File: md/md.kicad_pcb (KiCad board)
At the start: 2 copper layers, 49.5 x 70.5 mm, 53 parts, among them J1 ControlPort, J2 Conn_01x01, J3 Conn_02x08_Counter_Clockwise, J4 Conn_02x08_Counter_Clockwise, J5 Conn_01x01, J6 Conn_02x08_Counter_Clockwise, J7 Conn_02x08_Counter_Clockwise, J8 12v, Q1 FET_A_UP, Q2 FET_A_DOWN, Q3 FET_B_UP, Q4 FET_B_DOWN, U1 7400, U2 IRS2302, U3 TLP2955, U4 TLP2955, U5 IRS2302, U6 LM7812

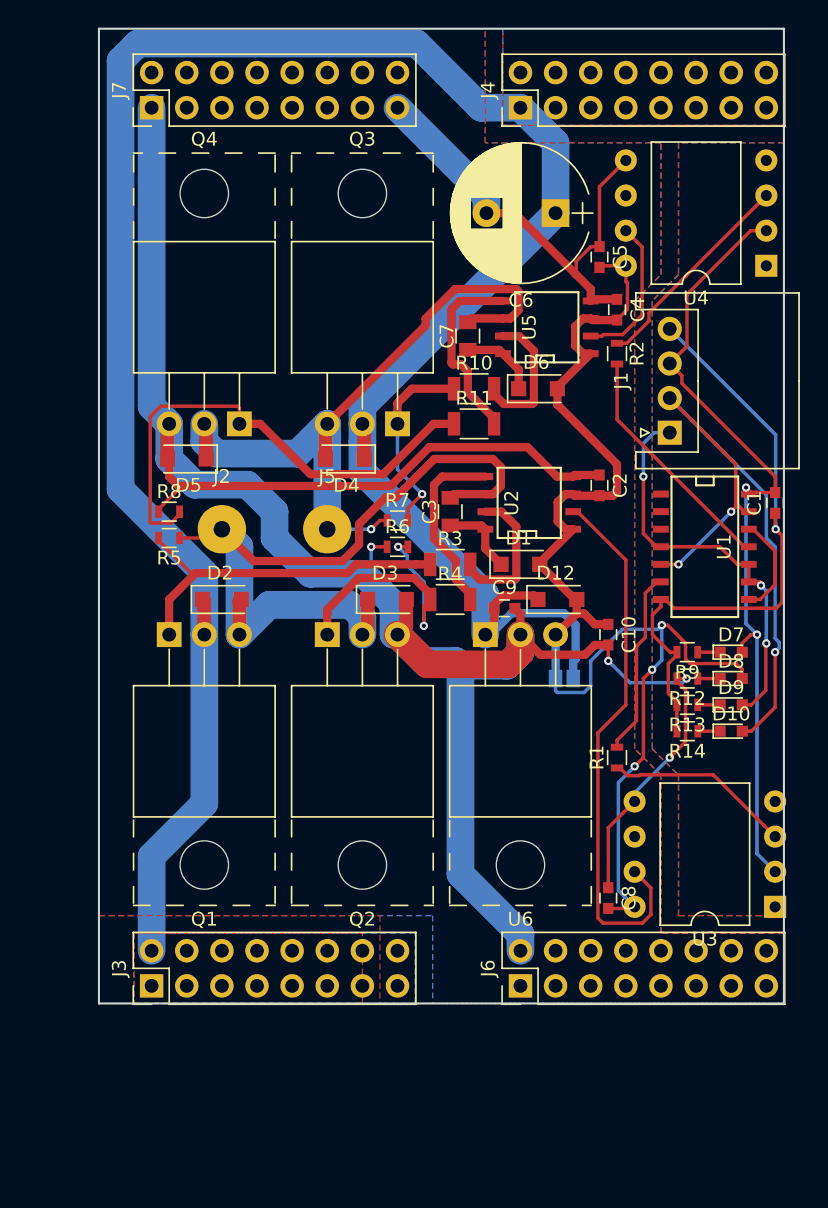
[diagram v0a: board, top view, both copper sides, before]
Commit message: use TLP2105
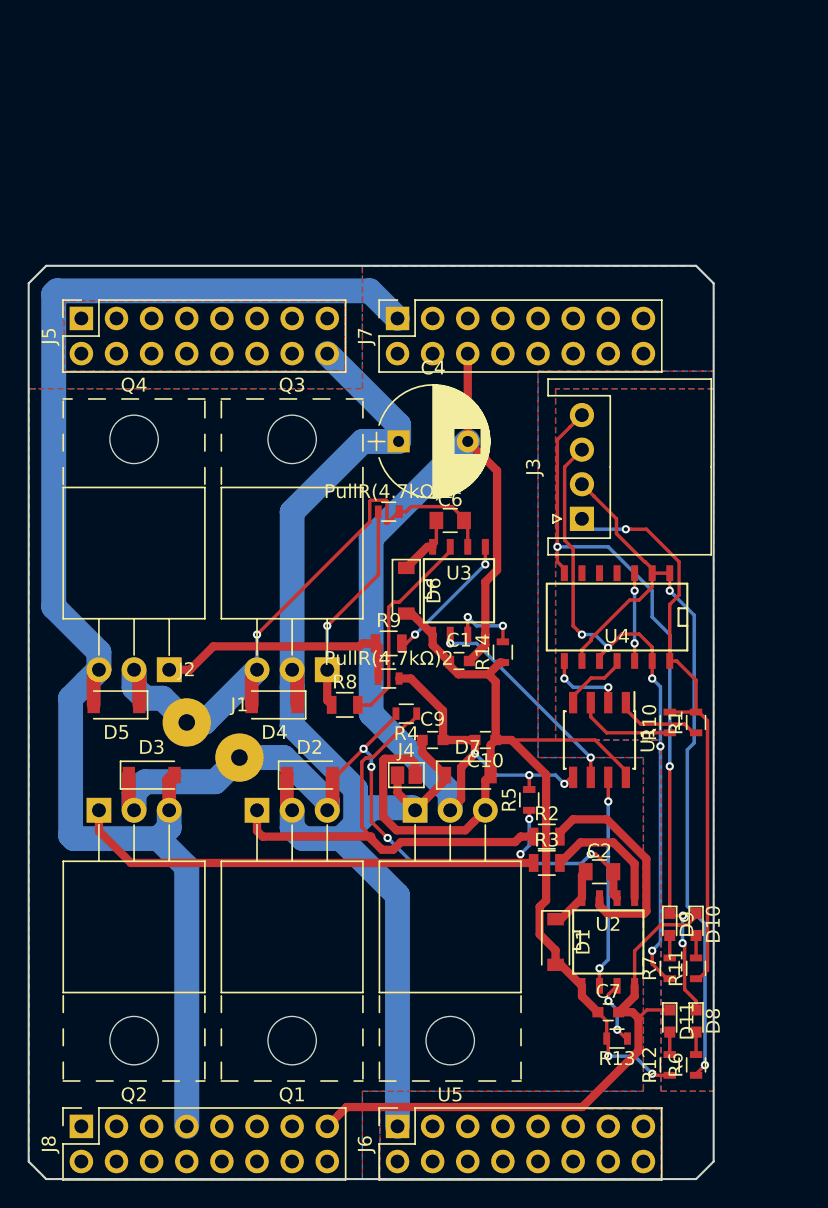
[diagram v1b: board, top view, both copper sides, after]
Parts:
- removed C3: bootC, Capacitors_SMD:C_0805
- removed C5, C8: passC, Capacitors_SMD:C_0603
- removed D12: RegRevD, Diodes_SMD:D_SOD-123F
- removed U6: LM7812, TO_SOT_Packages_THT:TO-220-3_Horizontal_Reversed
- added D11: SML-E12V8WT86, LEDs:LED_0603, F.Cu at (173.4, 149.9)
- added PullR(4.7kΩ)1: R, Resistors_SMD:R_0603, F.Cu at (153.0, 113.0)
- added PullR(4.7kΩ)2: R, Resistors_SMD:R_0603, F.Cu at (153.0, 125.1)
- C1: value passC -> 0.1uF
- C10: value RegOutC -> 1uF
- C2: value passC -> 10uF; footprint Capacitors_SMD:C_0603 -> Capacitors_SMD:C_0805
- C4: value passC -> CP; footprint Capacitors_SMD:C_0603 -> Capacitors_THT:CP_Radial_D8.0mm_P5.00mm
- C6: value PowerCP -> 10uF; footprint Capacitors_THT:CP_Radial_D10.0mm_P5.00mm -> Capacitors_SMD:C_0805
- C7: value bootC -> 0.1uF; footprint Capacitors_SMD:C_0805 -> Capacitors_SMD:C_0603
- C9: value RegInC -> 1uF
- D1, D6: value bootD -> SS2040FL; footprint Diodes_SMD:D_SOD-123F -> Diodes_SMD:D_SOD-123
- D10: value LED -> SML-E12P8T86
- D2, D3, D4, D5: value RevD -> SS2040FL; footprint Diodes_SMD:D_SOD-123F -> Diodes_SMD:D_SOD-123
- D7: value LED -> SS2040FL; footprint LEDs:LED_0603 -> Diodes_SMD:D_SOD-123
- D8: value LED -> SML-E12Y8WT86
- D9: value LED -> SML-E13BC8TT86
- J1: value ControlPort -> OutB; footprint Connectors_JST:JST_XH_S04B-XH-A_04x2.50mm_Angled -> Wire_Pads:SolderWirePad_single_1-2mmDrill
- J2: value Conn_01x01 -> OutA
- J3: value Conn_02x08_Counter_Clockwise -> Conn_01x04; footprint Pin_Headers:Pin_Header_Straight_2x08_Pitch2.54mm -> Connectors_JST:JST_XH_S04B-XH-A_04x2.50mm_Angled
- J4: value Conn_02x08_Counter_Clockwise -> GS2; footprint Pin_Headers:Pin_Header_Straight_2x08_Pitch2.54mm -> Connectors:GS2
- J5: value Conn_01x01 -> Conn_02x08_Counter_Clockwise; footprint Wire_Pads:SolderWirePad_single_1-2mmDrill -> Socket_Strips:Socket_Strip_Straight_2x08_Pitch2.54mm
- J6, J7: footprint Pin_Headers:Pin_Header_Straight_2x08_Pitch2.54mm -> Socket_Strips:Socket_Strip_Straight_2x08_Pitch2.54mm
- J8: value 12v -> Conn_02x08_Counter_Clockwise; footprint Connectors:GS2 -> Socket_Strips:Socket_Strip_Straight_2x08_Pitch2.54mm; moved to F.Cu
- Q1: value FET_A_UP -> IRFB7437PBF
- Q2: value FET_A_DOWN -> IRFB7437PBF
- Q3: value FET_B_UP -> IRFB7437PBF
- Q4: value FET_B_DOWN -> IRFB7437PBF
- R1: value tlp-in-R -> TLP_R(470Ω)
- R10: value GateR -> TLP_R(470Ω); footprint Resistors_SMD:R_1206 -> Resistors_SMD:R_0603
- R11: value GateR -> LEDR(470Ω); footprint Resistors_SMD:R_1206 -> Resistors_SMD:R_0603
- R12: value R -> LEDR(1.2kΩ)
- R13: value R -> PullR
- R2: value tlp-in-R -> GateR(6.8Ω); footprint Resistors_SMD:R_0603 -> Resistors_SMD:R_0805
- R3: value GateR -> GateR(6.8Ω); footprint Resistors_SMD:R_1206 -> Resistors_SMD:R_0805
- R4: value GateR -> PullR(4.7kΩ); footprint Resistors_SMD:R_1206 -> Resistors_SMD:R_0603
- R5: value PullR -> PullR(4.7kΩ)
- R6, R7: value PullR -> LEDR(470Ω)
- R8: value PullR -> GateR(6.8Ω); footprint Resistors_SMD:R_0603 -> Resistors_SMD:R_0805
- R9: value LEDR -> GateR(6.8Ω); footprint Resistors_SMD:R_0603 -> Resistors_SMD:R_0805
- U1: value 7400 -> TLP2105; footprint SMD_Packages:SOIC-14_N -> Housings_SOIC:SOIC-8_3.9x4.9mm_Pitch1.27mm
- U3: value TLP2955 -> IRS2302; footprint Housings_DIP:DIP-8_W10.16mm -> SMD_Packages:SOIC-8-N
- U4: value TLP2955 -> 7400; footprint Housings_DIP:DIP-8_W10.16mm -> SMD_Packages:SOIC-14_N
- U5: value IRS2302 -> L7812; footprint SMD_Packages:SOIC-8-N -> TO_SOT_Packages_THT:TO-220-3_Horizontal_Reversed
- moved C7 49.9 mm to (168.9, 149.2), turned to 0 degrees
- moved J4 49.0 mm to (154.3, 132.1)
- moved J8 47.6 mm to (130.8, 157.5), turned to 90 degrees
- moved J3 45.9 mm to (167.0, 113.5)
- moved R6 43.2 mm to (175.3, 153.0), turned to 90 degrees
- moved R11 42.5 mm to (175.3, 146.1), turned to 90 degrees
- moved J1 39.0 mm to (142.2, 130.8), turned to 0 degrees
- moved R7 37.9 mm to (173.4, 146.1), turned to 90 degrees
- moved U5 36.2 mm to (154.9, 134.6), turned to 0 degrees
- moved R2 35.3 mm to (164.5, 136.5), turned to 0 degrees
- moved U3 32.3 mm to (158.1, 118.7), turned to 0 degrees
- moved U2 32.3 mm to (168.9, 144.1), turned to 0 degrees
- moved R5 32.2 mm to (163.2, 133.9), turned to 90 degrees
- moved R10 28.0 mm to (173.4, 128.3), turned to 90 degrees
- moved R12 28.0 mm to (173.4, 153.0), turned to 90 degrees
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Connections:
- C1 pad 1: GND -> +12V
- C1 pad 2: +5V -> GNDPWR
- C2 pad 1: GNDPWR -> Net-(C2-Pad1)
- C2 pad 2: +12V -> Net-(C2-Pad2)
- C4 pad 1: GNDPWR -> +24V
- C4 pad 2: +12V -> GNDPWR
- C6 pad 1: +24V -> Net-(C6-Pad1)
- C6 pad 2: GNDPWR -> Net-(C6-Pad2)
- C7 pad 1: Net-(C7-Pad1) -> +12V
- C7 pad 2: Net-(C7-Pad2) -> GNDPWR
- D1 pad 1: Net-(C3-Pad1) -> Net-(C2-Pad1)
- D10 pad 1: Net-(D10-Pad1) -> GNDPWR
- D10 pad 2: /PWM -> Net-(D10-Pad2)
- D2 pad 2: Net-(C3-Pad2) -> Net-(C2-Pad2)
- D3 pad 1: Net-(C3-Pad2) -> Net-(C2-Pad2)
- D4 pad 2: Net-(C7-Pad2) -> Net-(C6-Pad2)
- D5 pad 1: Net-(C7-Pad2) -> Net-(C6-Pad2)
- D6 pad 1: Net-(C7-Pad1) -> Net-(C6-Pad1)
- D7 pad 1: Net-(D7-Pad1) -> +24V
- D7 pad 2: +5V -> +12V
- D8 pad 1: Net-(D8-Pad1) -> GND
- D8 pad 2: +12V -> Net-(D8-Pad2)
- D9 pad 1: Net-(D9-Pad1) -> GND
- D9 pad 2: /DIR -> Net-(D9-Pad2)
- J1 pad 1: /DIR -> Net-(C2-Pad2)
- J2 pad 1: Net-(C3-Pad2) -> Net-(C6-Pad2)
- J3 pad 1: +24V -> +5V
- J3 pad 2: +24V -> /DIR
- J3 pad 3: +24V -> /PWM
- J3 pad 4: +24V -> GND
- J4 pad 2: +24V -> +12V
- J5 pad 1: Net-(C7-Pad2) -> +24V
- J6 pad 1: GNDPWR -> +24V
- J6 pad 10: GNDPWR -> +24V
- J6 pad 11: GNDPWR -> +24V
- J6 pad 12: GNDPWR -> +24V
- J6 pad 13: GNDPWR -> +24V
- J6 pad 14: GNDPWR -> +24V
- J6 pad 15: GNDPWR -> +24V
- J6 pad 16: GNDPWR -> +24V
- J6 pad 2: GNDPWR -> +24V
- J6 pad 3: GNDPWR -> +24V
- J6 pad 4: GNDPWR -> +24V
- J6 pad 5: GNDPWR -> +24V
- J6 pad 6: GNDPWR -> +24V
- J6 pad 7: GNDPWR -> +24V
- J6 pad 8: GNDPWR -> +24V
- J6 pad 9: GNDPWR -> +24V
- J8 pad 1: +12V -> GNDPWR
- J8 pad 2: +24V -> GNDPWR
- Q1 pad 3: Net-(C3-Pad2) -> Net-(C2-Pad2)
- Q2 pad 2: Net-(C3-Pad2) -> Net-(C2-Pad2)
- Q3 pad 1: Net-(Q3-Pad1) -> Net-(PullR(4.7kΩ)1-Pad1)
- Q3 pad 3: Net-(C7-Pad2) -> Net-(C6-Pad2)
- Q4 pad 1: Net-(Q4-Pad1) -> Net-(PullR(4.7kΩ)2-Pad1)
- Q4 pad 2: Net-(C7-Pad2) -> Net-(C6-Pad2)
- R1 pad 2: Net-(R1-Pad2) -> +5V
- R10 pad 1: Net-(Q3-Pad1) -> Net-(R10-Pad1)
- R10 pad 2: Net-(R10-Pad2) -> +5V
- R11 pad 1: Net-(Q4-Pad1) -> +5V
- R11 pad 2: Net-(R11-Pad2) -> Net-(D10-Pad2)
- R12 pad 1: Net-(D8-Pad1) -> +12V
- R12 pad 2: GNDPWR -> Net-(D11-Pad2)
- R13 pad 1: Net-(D9-Pad1) -> Net-(R13-Pad1)
- R13 pad 2: GND -> +12V
- R14 pad 1: Net-(D10-Pad1) -> +12V
- R14 pad 2: GND -> Net-(R14-Pad2)
- R2 pad 1: Net-(R2-Pad1) -> Net-(Q1-Pad1)
- R3 pad 1: Net-(Q1-Pad1) -> Net-(Q2-Pad1)
- R4 pad 1: Net-(Q2-Pad1) -> Net-(Q1-Pad1)
- R4 pad 2: Net-(R4-Pad2) -> Net-(C2-Pad2)
- R5 pad 1: Net-(C3-Pad2) -> Net-(Q2-Pad1)
- R5 pad 2: Net-(Q1-Pad1) -> GNDPWR
- R6 pad 1: GNDPWR -> /DIR
- R6 pad 2: Net-(Q2-Pad1) -> Net-(D8-Pad2)
- R7 pad 1: Net-(C7-Pad2) -> /PWM
- R7 pad 2: Net-(Q3-Pad1) -> Net-(D9-Pad2)
- R8 pad 1: GNDPWR -> Net-(PullR(4.7kΩ)1-Pad1)
- R8 pad 2: Net-(Q4-Pad1) -> Net-(R8-Pad2)
- R9 pad 1: Net-(D7-Pad1) -> Net-(PullR(4.7kΩ)2-Pad1)
- R9 pad 2: GND -> Net-(R9-Pad2)
- U1 pad 1: Net-(U1-Pad1) -> Net-(R1-Pad1)
- U1 pad 3: Net-(U1-Pad3) -> Net-(R10-Pad1)
- U1 pad 4: /DIR -> Net-(U1-Pad4)
- U1 pad 5: /PWM -> GNDPWR
- U1 pad 6: Net-(R1-Pad2) -> /OUTB
- U1 pad 7: GND -> /OUTA
- U1 pad 8: Net-(U1-Pad12) -> +12V
- U2 pad 2: OUTA -> /OUTA
- U2 pad 3: +12V -> Net-(R13-Pad1)
- U2 pad 5: Net-(R4-Pad2) -> Net-(R3-Pad2)
- U2 pad 6: Net-(C3-Pad2) -> Net-(C2-Pad2)
- U2 pad 7: Net-(R3-Pad2) -> Net-(R2-Pad2)
- U2 pad 8: Net-(C3-Pad1) -> Net-(C2-Pad1)
- U3 pad 1: (no net) -> +12V
- U3 pad 2: +5V -> /OUTB
- U3 pad 3: Net-(R1-Pad1) -> Net-(R14-Pad2)
- U3 pad 4: (no net) -> GNDPWR
- U3 pad 5: GNDPWR -> Net-(R9-Pad2)
- U3 pad 6: (no net) -> Net-(C6-Pad2)
- U3 pad 7: OUTA -> Net-(R8-Pad2)
- U3 pad 8: +12V -> Net-(C6-Pad1)
- U4 pad 1: (no net) -> /DIR
- U4 pad 2: +5V -> /DIR
- U4 pad 3: Net-(R2-Pad1) -> Net-(U4-Pad12)
- U4 pad 4: (no net) -> Net-(U4-Pad4)
- U4 pad 5: GNDPWR -> Net-(U4-Pad5)
- U4 pad 6: (no net) -> Net-(U4-Pad6)
- U4 pad 7: OUTB -> GND
- U4 pad 8: +12V -> Net-(U1-Pad2)
- U5 pad 1: +12V -> +24V
- U5 pad 2: OUTB -> GNDPWR
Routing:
- net +24V: track 171.1 -> 91.9 mm
- net Net-(C3-Pad2): track 59.4 -> 0.00 mm
- net Net-(C2-Pad2): track 0.00 -> 57.3 mm, vias 0 -> 4
- net Net-(C7-Pad2): track 52.4 -> 0.00 mm, vias 1 -> 0
- net Net-(C6-Pad2): track 0.00 -> 45.3 mm, vias 0 -> 1
- net OUTA: track 39.8 -> 0.00 mm
- net Net-(Q4-Pad1): track 36.7 -> 0.00 mm
- net /DIR: track 29.6 -> 56.7 mm, vias 3 -> 2
- net Net-(PullR(4.7kΩ)2-Pad1): track 0.00 -> 18.3 mm
- net Net-(Q2-Pad1): track 20.3 -> 38.0 mm
- net +5V: track 58.9 -> 42.6 mm, vias 2 -> 1
- net /OUTB: track 0.00 -> 15.6 mm, vias 0 -> 2
- net Net-(PullR(4.7kΩ)1-Pad1): track 0.00 -> 15.6 mm, vias 0 -> 1
- net Net-(R2-Pad1): track 15.6 -> 0.00 mm
- net /OUTA: track 0.00 -> 15.3 mm, vias 0 -> 2
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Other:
- board size 49.5 x 70.5 mm -> 49.5 x 66 mm

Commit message: だいたい配置出来た
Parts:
- added C11: C, Capacitors_SMD:C_0603, F.Cu at (212.7, 78.1)
- added C3: PowerC, Capacitors_THT:C_Disc_D5.0mm_W2.5mm_P5.00mm, F.Cu at (207.0, 88.9)
- added C5: PowerC, Capacitors_THT:C_Disc_D5.0mm_W2.5mm_P5.00mm, F.Cu at (209.6, 95.2)
- added C8: C, Capacitors_SMD:C_0603, F.Cu at (229.9, 88.3)
- C10: value 1uF -> RegOutC(1uF)
- C2, C6: value 10uF -> BootC(10uF); footprint Capacitors_SMD:C_0805 -> Capacitors_SMD:C_1206
- C4: value CP -> PowerCP
- C9: value 1uF -> RegInC(1uF)
- D10: value SML-E12P8T86 -> 5VLED(SML-E12P8T86)
- D11: value SML-E12V8WT86 -> 12VLED(SML-E12V8WT86)
- D2, D3, D4, D5: value SS2040FL -> RevD(SS2040FL)
- D7: value SS2040FL -> RegRevC(SS2040FL)
- D8: value SML-E12Y8WT86 -> DIRLED(SML-E12Y8WT86)
- D9: value SML-E13BC8TT86 -> LED(SML-E13BC8TT86)
- J3: value Conn_01x04 -> Interface
- J4: value GS2 -> 12VJmp
- Q1, Q2: value IRFB7437PBF -> FETA(IRFB7437PBF)
- Q3, Q4: value IRFB7437PBF -> FETB(IRFB7437PBF)
- R11: value LEDR(470Ω) -> 5VLEDR(470Ω)
- R12: value LEDR(1.2kΩ) -> 12VLEDR(1.2kΩ)
- R14: value R -> PullR
- R2, R3, R8, R9: value GateR(6.8Ω) -> GateR(8.2Ω); footprint Resistors_SMD:R_0805 -> Resistors_SMD:R_1206
- R6: value LEDR(470Ω) -> DIRLEDR(470Ω)
- R7: value LEDR(470Ω) -> PWMLEDR(470Ω)
- U1: footprint Housings_SOIC:SOIC-8_3.9x4.9mm_Pitch1.27mm -> SMD_Packages:SOIC-8-N
- U2, U3: value IRS2302 -> IR7184S
- moved J5 90.9 mm to (213.4, 61.0)
- moved J8 90.4 mm to (213.4, 120.7)
- moved C2 85.8 mm to (215.3, 67.3)
- moved R13 85.6 mm to (215.3, 78.7)
- moved U2 85.2 mm to (216.0, 73.2)
- moved D1 84.9 mm to (211.5, 73.0)
- moved R12 83.3 mm to (229.2, 91.3), turned to 270 degrees
- moved D8 80.5 mm to (219.1, 82.4)
- moved R6 80.4 mm to (219.1, 85.6), turned to 270 degrees
- moved Q1 79.8 mm to (207.0, 86.4), turned to 180 degrees
- moved R8 79.8 mm to (225.2, 101.0)
- moved Q2 78.8 mm to (194.3, 86.4), turned to 180 degrees
- moved D11 78.5 mm to (229.2, 94.8), turned to 90 degrees
- moved R11 78.1 mm to (231.1, 91.4)
- moved D6 76.7 mm to (230.6, 110.5), turned to 90 degrees
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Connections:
- J3 pad 1: +5V -> GND
- J3 pad 2: /DIR -> +5V
- J3 pad 4: GND -> /DIR
- U2 pad 5: Net-(R3-Pad2) -> Net-(R2-Pad2)
- U2 pad 7: Net-(R2-Pad2) -> Net-(R3-Pad2)
- U3 pad 5: Net-(R9-Pad2) -> Net-(R8-Pad2)
- U3 pad 7: Net-(R8-Pad2) -> Net-(R9-Pad2)
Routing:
- net +24V: track 91.9 -> 161.8 mm
- net /DIR: track 56.7 -> 0.00 mm, vias 2 -> 0
- net +12V: track 79.3 -> 23.7 mm, vias 2 -> 0
- net GND: track 52.7 -> 0.00 mm, vias 4 -> 0
- net /PWM: track 48.2 -> 0.00 mm, vias 5 -> 0
- net +5V: track 42.6 -> 0.00 mm, vias 1 -> 0
- net Net-(C6-Pad2): track 45.3 -> 81.1 mm, vias 1 -> 0
- net GNDPWR: track 224.4 -> 188.7 mm, vias 3 -> 1
- net Net-(PullR(4.7kΩ)2-Pad1): track 18.3 -> 47.4 mm
- net Net-(Q1-Pad1): track 33.8 -> 11.7 mm
- net /OUTB: track 15.6 -> 0.00 mm, vias 2 -> 0
- net /OUTA: track 15.3 -> 0.00 mm, vias 2 -> 0
- net Net-(PullR(4.7kΩ)1-Pad1): track 15.6 -> 30.3 mm, vias 1 -> 0
- net Net-(R3-Pad2): track 9.14 -> 20.9 mm
- net Net-(Q2-Pad1): track 38.0 -> 28.9 mm, vias 2 -> 1
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- removed copper zone on B.Cu, net +24V
- removed copper zone on F.Cu, net +24V
- removed copper zone on B.Cu, net GND
- removed copper zone on F.Cu, net GND
- removed copper zone on B.Cu, net GNDPWR
- removed copper zone on F.Cu, net GNDPWR
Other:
- board size 49.5 x 66 mm -> 59.7 x 67.3 mm

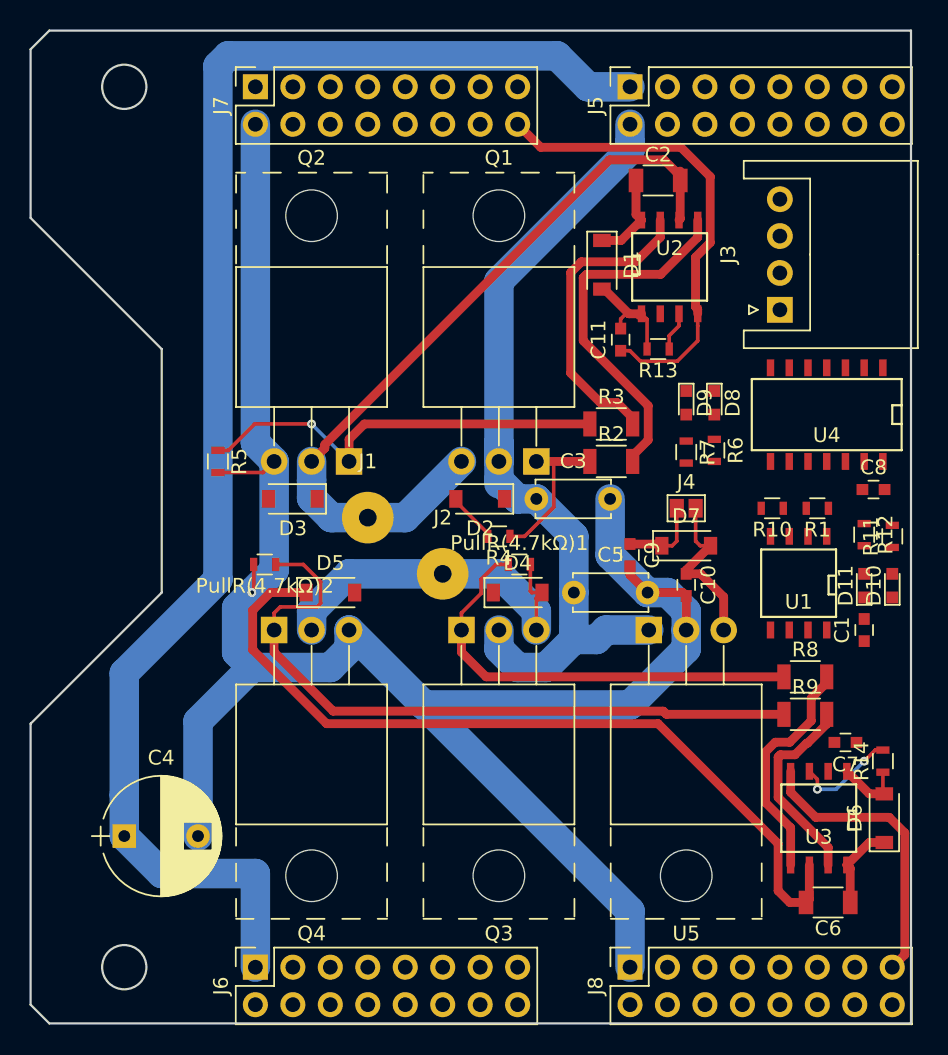
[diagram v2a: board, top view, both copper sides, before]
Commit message: drew pcb pattern
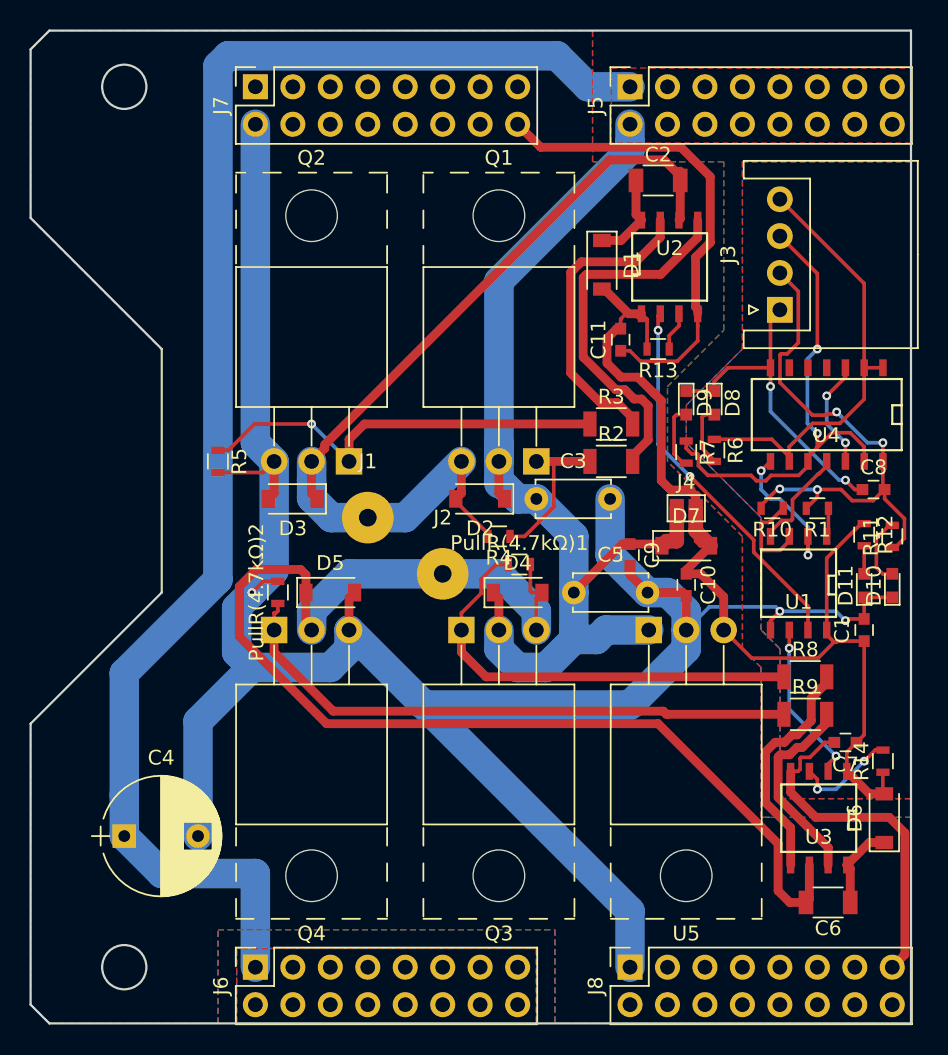
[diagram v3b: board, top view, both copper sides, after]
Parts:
- moved PullR(4.7kΩ)2 2.09 mm to (189.5, 95.2), turned to 90 degrees
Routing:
- net +12V: track 23.7 -> 72.9 mm
- net +5V: track 0.00 -> 38.2 mm, vias 0 -> 4
- net /PWM: track 0.00 -> 33.0 mm, vias 0 -> 2
- net /DIR: track 0.00 -> 30.2 mm
- net GNDPWR: track 188.7 -> 216.5 mm, vias 1 -> 3
- net /OUTA: track 0.00 -> 25.7 mm, vias 0 -> 2
- net GND: track 0.00 -> 22.3 mm, vias 0 -> 2
- net +24V: track 161.8 -> 173.1 mm
- net /OUTB: track 0.00 -> 11.1 mm, vias 0 -> 2
- net Net-(U1-Pad2): track 0.00 -> 9.57 mm, vias 0 -> 2
- net Net-(PullR(4.7kΩ)2-Pad1): track 47.4 -> 39.8 mm
- net Net-(U4-Pad12): track 0.00 -> 7.40 mm, vias 0 -> 2
- net Net-(U1-Pad4): track 0.00 -> 7.07 mm
- net Net-(C6-Pad2): track 81.1 -> 88.0 mm
- net Net-(R10-Pad1): track 0.00 -> 6.18 mm
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- added copper zone on B.Cu, net +24V
- added copper zone on F.Cu, net +24V
- added copper zone on B.Cu, net GND
- added copper zone on F.Cu, net GND
- added copper zone on B.Cu, net GNDPWR
- added copper zone on F.Cu, net GNDPWR
